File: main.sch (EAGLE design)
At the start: 108 parts, among them IC1 LD1117S50TR, IC2 LD398533RM, IC3 CP2102, IC4 PM8834-SO08N, IC5 PM8834-SO08N, J1 RJ11, Q10 IRF3205SPBF, Q11 IRF3205SPBF, Q12 IRF3205SPBF, Q13 IRF3205SPBF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

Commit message: All routed
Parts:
- removed JP3, JP4: (no value), adafruit:PINHD-1X3
- removed Q4, Q5: BSS138, SparkFun:MOSFET-NCHANNELSMD
- removed R17, R18, R19, R20: 10K, resistor:R-EU_R0805
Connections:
- removed net HV: JP2.1, JP3.1, JP4.1, R16.1, R18.1, R20.1
- removed net HV3: JP3.2, Q4.D, R18.2
- removed net HV4: JP4.2, Q5.D, R20.2
- removed net LV2: Q4.S, R17.2
- removed net LV3: Q5.S, R19.2
- net +3V3: no longer Q4.G, Q5.G, R17.1, R19.1
- net +5V: now also JP2.1, R16.1
- net GND: no longer JP3.3, JP4.3
- net LV0: now also U1.IO15
- net LV1: now also U1.IO16

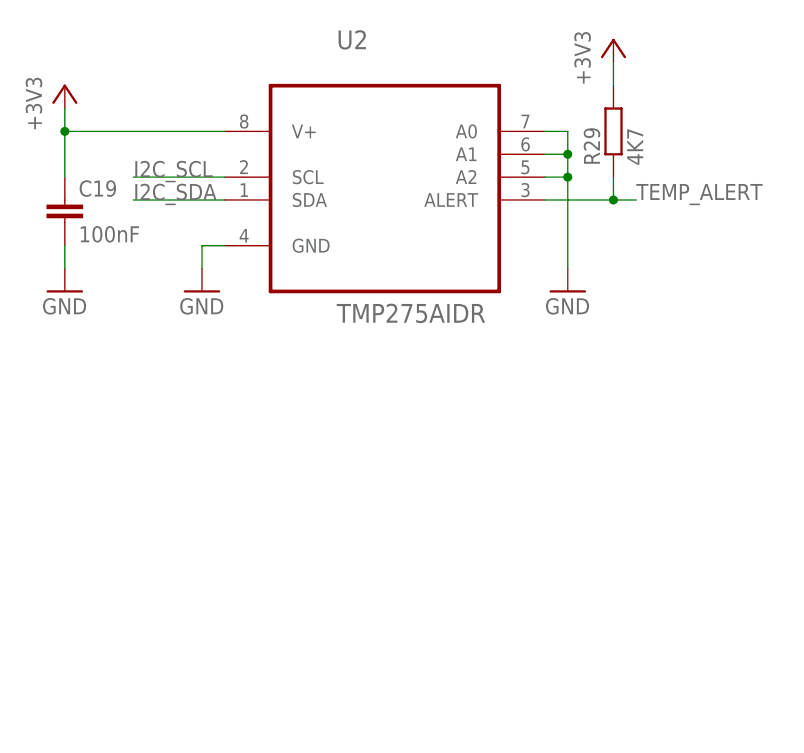
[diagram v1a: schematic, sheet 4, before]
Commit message: Added light sensor
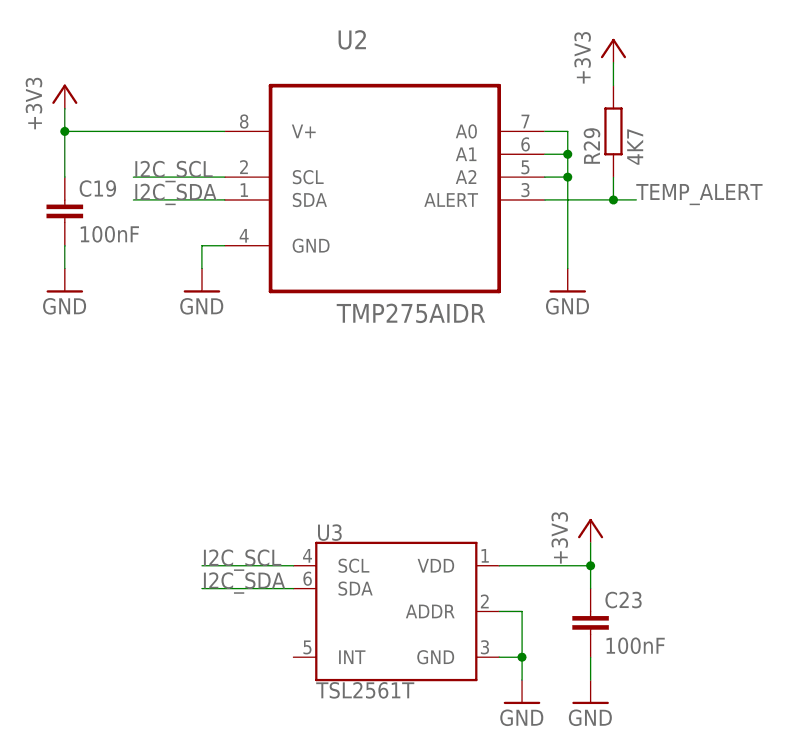
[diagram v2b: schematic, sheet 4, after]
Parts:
- added C23: 100nF, resistor:C-EUC0805
- added U3: TSL2561T, SparkFun-Sensors:TSL2561T
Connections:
- net +3V3: now also C23.1, U3.VDD
- net GND: now also C23.2, U3.ADDR, U3.GND
- net I2C_SCL: now also U3.SCL
- net I2C_SDA: now also U3.SDA
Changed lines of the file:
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@@
 <part name="P+9" library="supply1" library_urn="urn:adsk.eagle:library:371" deviceset="+5V" device=""/>
 <part name="P+5" library="supply1" library_urn="urn:adsk.eagle:library:371" deviceset="+5V" device=""/>
+<part name="U3" library="SparkFun-Sensors" library_urn="urn:adsk.eagle:library:534" deviceset="TSL2561" device="T" package3d_urn="urn:adsk.eagle:package:39968/1"/>
+<part name="GND32" library="supply1" deviceset="GND" device=""/>
+<part name="+3V1" library="supply1" deviceset="+3V3" device=""/>
+<part name="C23" library="resistor" deviceset="C-EU" device="C0805" value="100nF"/>
+<part name="GND33" library="supply1" deviceset="GND" device=""/>
 </parts>
 <sheets>
@@
 <attribute name="VALUE" x="76.2" y="60.96" size="1.778" layer="96" rot="R90"/>
 </instance>
+<instance part="U3" gate="G$1" x="53.34" y="2.54" smashed="yes">
+<attribute name="NAME" x="45.72" y="10.414" size="1.778" layer="95" font="vector"/>
+<attribute name="VALUE" x="45.72" y="-5.334" size="1.778" layer="96" font="vector" align="top-left"/>
+</instance>
+<instance part="GND32" gate="1" x="68.58" y="-7.62" smashed="yes">
+<attribute name="VALUE" x="66.04" y="-10.16" size="1.778" layer="96"/>
+</instance>
+<instance part="+3V1" gate="G$1" x="76.2" y="12.7" smashed="yes">
+<attribute name="VALUE" x="73.66" y="7.62" size="1.778" layer="96" rot="R90"/>
+</instance>
+<instance part="C23" gate="G$1" x="76.2" y="2.54" smashed="yes">
+<attribute name="NAME" x="77.724" y="2.921" size="1.778" layer="95"/>
+<attribute name="VALUE" x="77.724" y="-2.159" size="1.778" layer="96"/>
+</instance>
+<instance part="GND33" gate="1" x="76.2" y="-7.62" smashed="yes">
+<attribute name="VALUE" x="73.66" y="-10.16" size="1.778" layer="96"/>
+</instance>
 </instances>
 <busses>
@@
 <pinref part="GND44" gate="1" pin="GND"/>
 </segment>
+<segment>
+<pinref part="U3" gate="G$1" pin="ADDR"/>
+<wire x1="66.04" y1="2.54" x2="68.58" y2="2.54" width="0.1524" layer="91"/>
+<wire x1="68.58" y1="2.54" x2="68.58" y2="-2.54" width="0.1524" layer="91"/>
+<pinref part="U3" gate="G$1" pin="GND"/>
+<wire x1="68.58" y1="-2.54" x2="68.58" y2="-5.08" width="0.1524" layer="91"/>
+<wire x1="66.04" y1="-2.54" x2="68.58" y2="-2.54" width="0.1524" layer="91"/>
+<junction x="68.58" y="-2.54"/>
+<pinref part="GND32" gate="1" pin="GND"/>
+</segment>
+<segment>
+<pinref part="GND33" gate="1" pin="GND"/>
+<pinref part="C23" gate="G$1" pin="2"/>
+<wire x1="76.2" y1="-2.54" x2="76.2" y2="-5.08" width="0.1524" layer="91"/>
+</segment>
 </net>
 <net name="+3V3" class="0">
@@
 <pinref part="+3V320" gate="G$1" pin="+3V3"/>
 </segment>
+<segment>
+<pinref part="U3" gate="G$1" pin="VDD"/>
+<wire x1="66.04" y1="7.62" x2="76.2" y2="7.62" width="0.1524" layer="91"/>
+<wire x1="76.2" y1="7.62" x2="76.2" y2="10.16" width="0.1524" layer="91"/>
+<pinref part="+3V1" gate="G$1" pin="+3V3"/>
+<pinref part="C23" gate="G$1" pin="1"/>
+<wire x1="76.2" y1="5.08" x2="76.2" y2="7.62" width="0.1524" layer="91"/>
+<junction x="76.2" y="7.62"/>
+</segment>
 </net>
 <net name="I2C_SDA" class="0">
@@
 <label x="25.4" y="48.26" size="1.778" layer="95"/>
 </segment>
+<segment>
+<wire x1="33.02" y1="5.08" x2="43.18" y2="5.08" width="0.1524" layer="91"/>
+<pinref part="U3" gate="G$1" pin="SDA"/>
+<label x="33.02" y="5.08" size="1.778" layer="95"/>
+</segment>
 </net>
 <net name="I2C_SCL" class="0">
@@
 <label x="25.4" y="50.8" size="1.778" layer="95"/>
 </segment>
-</net>
+<segment>
+<wire x1="43.18" y1="7.62" x2="33.02" y2="7.62" width="0.1524" layer="91"/>
+<pinref part="U3" gate="G$1" pin="SCL"/>
+<label x="33.02" y="7.62" size="1.778" layer="95"/>
+</segment>
+</net>

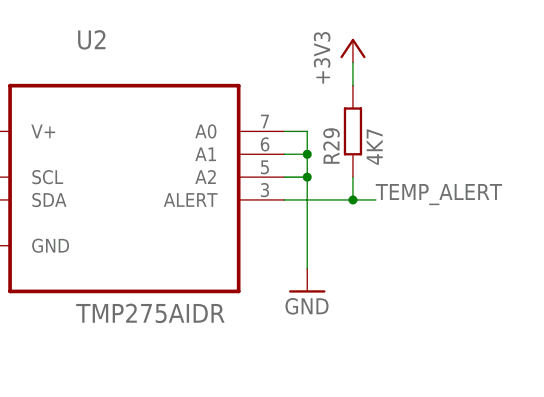
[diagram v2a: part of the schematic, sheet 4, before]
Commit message: Removed temp alert signal
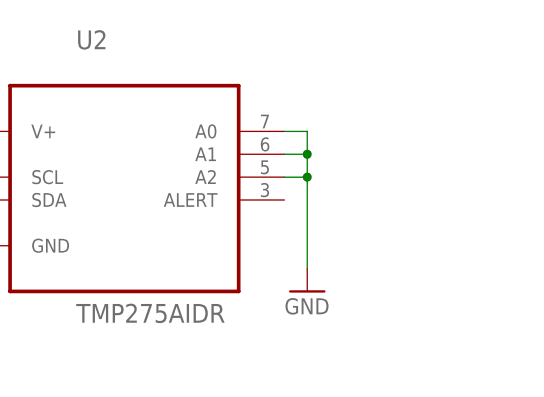
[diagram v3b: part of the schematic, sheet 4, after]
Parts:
- removed R29: 4K7, resistor:R-EU_R0805
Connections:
- removed net TEMP_ALERT: R29.1, U1.IO21, U2.ALERT
- net +3V3: no longer R29.2
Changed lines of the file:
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@@
 <part name="+3V39" library="supply1" library_urn="urn:adsk.eagle:library:371" deviceset="+3V3" device=""/>
 <part name="+3V310" library="supply1" library_urn="urn:adsk.eagle:library:371" deviceset="+3V3" device=""/>
-<part name="R29" library="resistor" library_urn="urn:adsk.eagle:library:348" deviceset="R-EU_" device="R0805" package3d_urn="urn:adsk.eagle:package:23553/2" value="4K7"/>
-<part name="+3V320" library="supply1" deviceset="+3V3" device=""/>
 <part name="GND25" library="supply1" library_urn="urn:adsk.eagle:library:371" deviceset="GND" device=""/>
 <part name="GND26" library="supply1" library_urn="urn:adsk.eagle:library:371" deviceset="GND" device=""/>
@@
 </segment>
 </net>
-<net name="TEMP_ALERT" class="0">
-<segment>
-<pinref part="U1" gate="G$1" pin="IO21"/>
-<wire x1="149.86" y1="73.66" x2="157.48" y2="73.66" width="0.1524" layer="91"/>
-<label x="154.94" y="73.66" size="1.778" layer="95"/>
-</segment>
-</net>
 <net name="INP2" class="0">
 <segment>
@@
 <instance part="GND44" gate="1" x="73.66" y="38.1" smashed="yes">
 <attribute name="VALUE" x="71.12" y="35.56" size="1.778" layer="96"/>
-</instance>
-<instance part="R29" gate="G$1" x="78.74" y="55.88" smashed="yes" rot="R90">
-<attribute name="NAME" x="77.2414" y="52.07" size="1.778" layer="95" rot="R90"/>
-<attribute name="VALUE" x="82.042" y="52.07" size="1.778" layer="96" rot="R90"/>
-</instance>
-<instance part="+3V320" gate="G$1" x="78.74" y="66.04" smashed="yes">
-<attribute name="VALUE" x="76.2" y="60.96" size="1.778" layer="96" rot="R90"/>
 </instance>
 <instance part="U3" gate="G$1" x="53.34" y="2.54" smashed="yes">
@@
 </segment>
 <segment>
-<pinref part="R29" gate="G$1" pin="2"/>
-<wire x1="78.74" y1="60.96" x2="78.74" y2="63.5" width="0.1524" layer="91"/>
-<pinref part="+3V320" gate="G$1" pin="+3V3"/>
-</segment>
-<segment>
 <pinref part="U3" gate="G$1" pin="VDD"/>
 <wire x1="66.04" y1="7.62" x2="76.2" y2="7.62" width="0.1524" layer="91"/>
@@
 </segment>
 </net>
-<net name="TEMP_ALERT" class="0">
-<segment>
-<pinref part="U2" gate="A" pin="ALERT"/>
-<wire x1="71.12" y1="48.26" x2="78.74" y2="48.26" width="0.1524" layer="91"/>
-<label x="81.28" y="48.26" size="1.778" layer="95"/>
-<pinref part="R29" gate="G$1" pin="1"/>
-<wire x1="78.74" y1="48.26" x2="81.28" y2="48.26" width="0.1524" layer="91"/>
-<wire x1="78.74" y1="48.26" x2="78.74" y2="50.8" width="0.1524" layer="91"/>
-<junction x="78.74" y="48.26"/>
-</segment>
-</net>

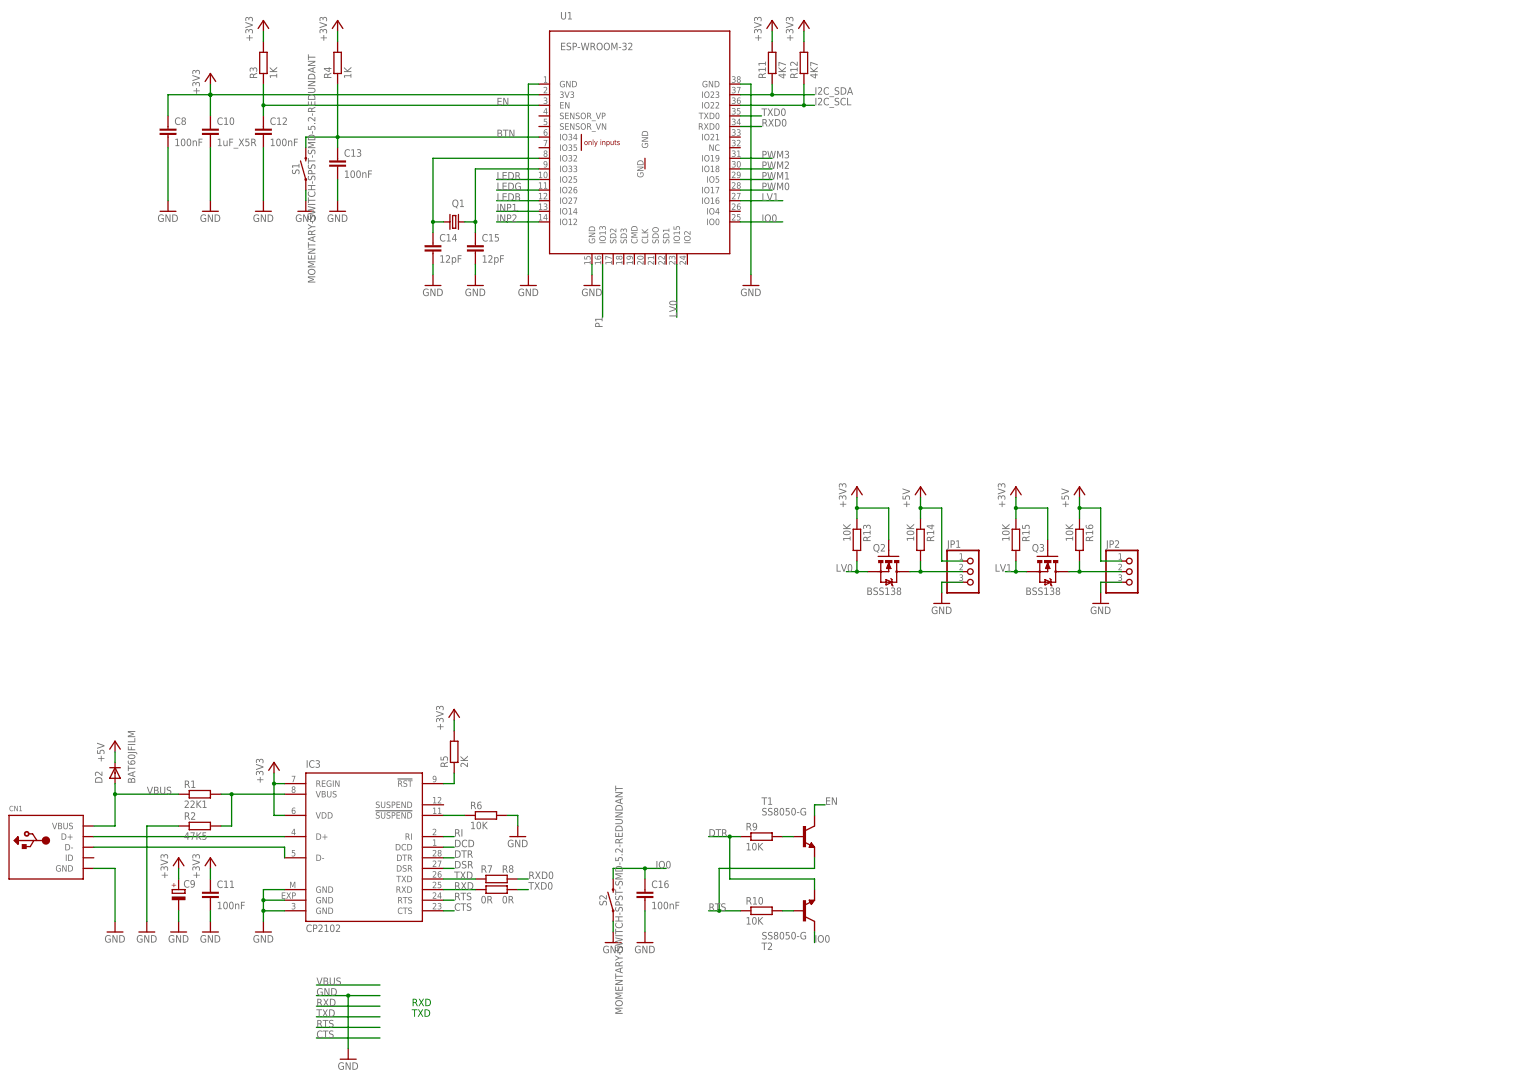
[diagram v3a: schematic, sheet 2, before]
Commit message: Replaced usb chip by connector
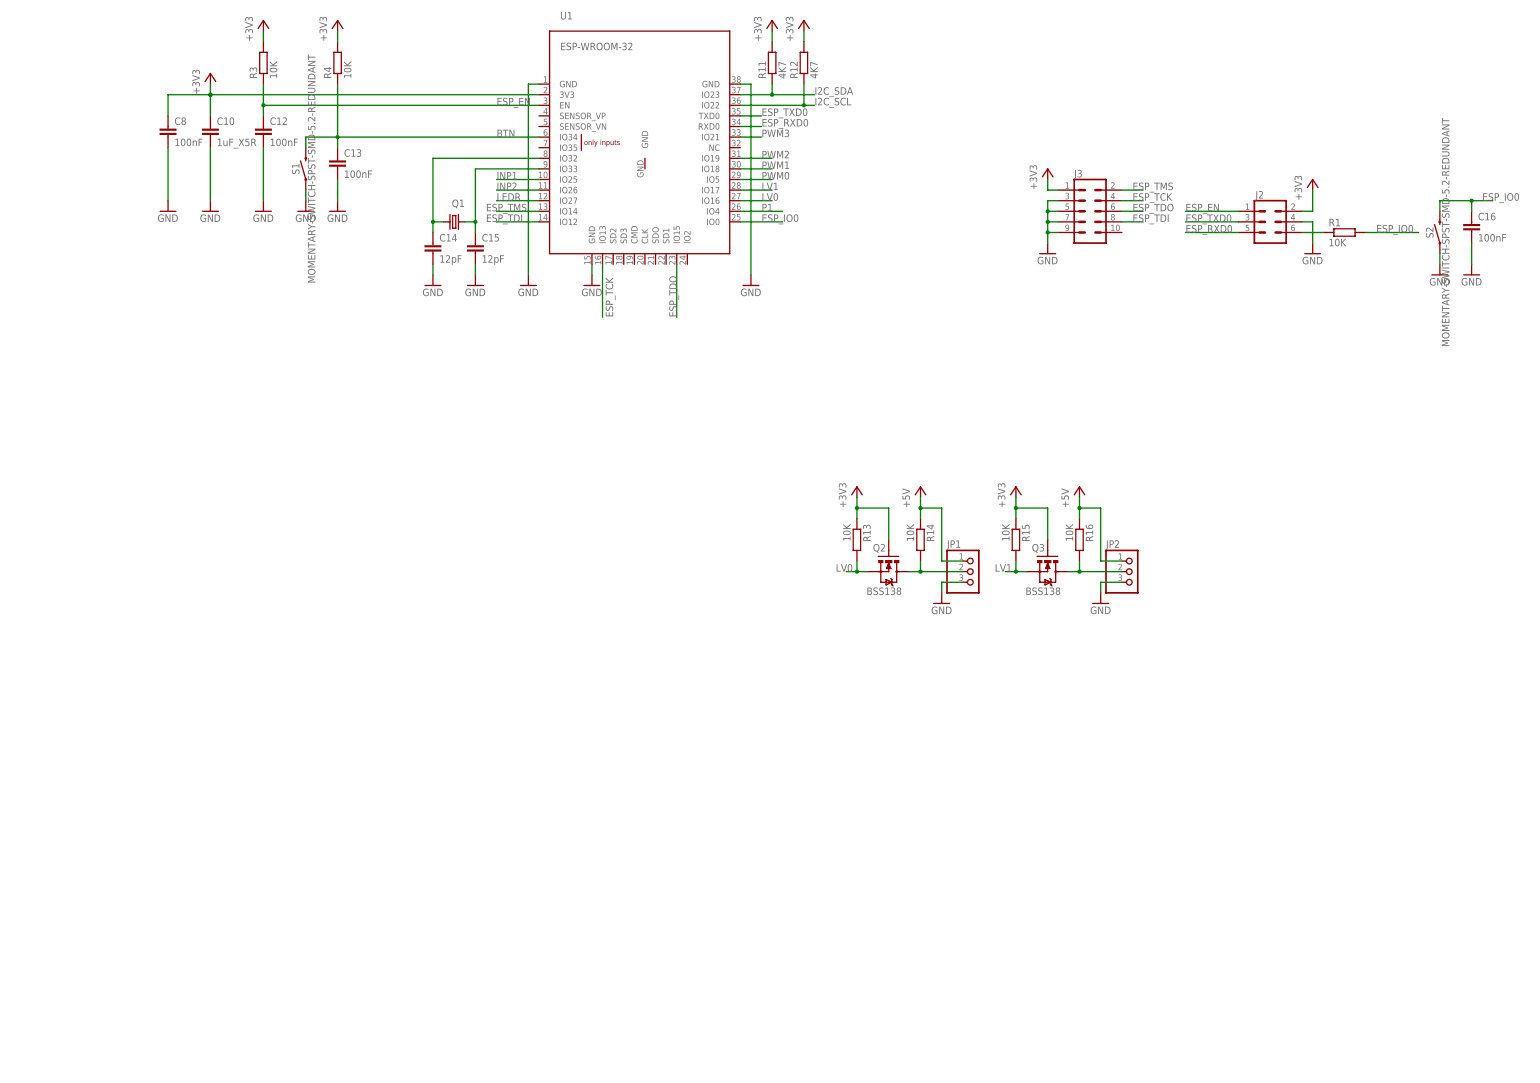
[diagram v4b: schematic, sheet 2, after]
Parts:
- removed C11: 100nF, resistor:C-EUC0805
- removed C9: (no value), resistor:CPOL-EUSMCA
- removed CN1: (no value), adafruit:USBMINIB
- removed D2: BAT60JFILM, diode:DIODE-SOD323-W
- removed IC3: CP2102, silabs:CP2102
- removed Q7, Q8: BSS138, SparkFun:MOSFET-NCHANNELSMD
- removed R10, R31, R32, R6, R9: 10K, resistor:R-EU_R0805
- removed R2: 47K5, resistor:R-EU_R0805
- removed R5: 2K, resistor:R-EU_R0805
- removed R7, R8: 0R, resistor:R-EU_R0805
- removed T1, T2: SS8050-G, transistor:BCF29-NPN-SOT23-BEC
- added J2: (no value), SparkFun-Connectors:CONN_03X2SHROUD
- added J3: (no value), SparkFun-Connectors:CONN_05X2SHD
- LED1: value RGBLED5050 -> RED; device adafruit:RGBLED5050 -> led:LEDCHIPLED_0805
- R1: value 22K1 -> 10K
- R3, R4: value 1K -> 10K
- R30: value 10K -> 1K
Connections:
- removed net CTS: IC3.CTS
- removed net DCD: IC3.DCD
- removed net DSR: IC3.DSR
- removed net DTR: IC3.DTR, R9.1, T2.E
- removed net EN: C12.1, R3.1, T1.C, U1.EN
- removed net IO0: C16.1, S2.2, T2.C, U1.IO0
- removed net LEDB: Q8.G, U1.IO27
- removed net LEDG: Q7.G, U1.IO26
- removed net N$11: LED1.RED_C, R31.1
- removed net N$19: IC3.!SUSPEND, R6.1
- removed net N$21: IC3.!RST, R5.1
- removed net N$24: IC3.VBUS, R1.2, R2.2
- removed net N$25: CN1.D-, IC3.D-
- removed net N$29: LED1.BLUE_C, R32.1
- removed net N$31: Q7.D, R31.2
- removed net N$32: Q8.D, R32.2
- removed net N$42: R9.2, T1.B
- removed net N$43: R10.2, T2.B
- removed net N$6: CN1.D+, IC3.D+
- removed net RI: IC3.RI
- removed net RTS: IC3.RTS, R10.1, T1.E
- removed net RXD: IC3.RXD, R8.1
- removed net RXD0: R7.2, U1.RXD0
- removed net TXD: IC3.TXD, R7.1
- removed net TXD0: R8.2, U1.TXD0
- removed net VBUS: CN1.VBUS, D2.A, R1.1
- new net ESP_EN: C12.1, J2.1, R3.1, U1.EN
- new net ESP_IO0: C16.1, R1.2, S2.2, U1.IO0
- new net ESP_RXD0: J2.5, U1.RXD0
- new net ESP_TCK: J3.4, U1.IO13
- new net ESP_TDI: J3.8, U1.IO12
- new net ESP_TDO: J3.6, U1.IO15
- new net ESP_TMS: J3.2, U1.IO14
- new net ESP_TXD0: J2.3, U1.TXD0
- new net N$4: J2.6, R1.1
- net +3V3: now also J2.2, J3.1, LED1.A; no longer C11.1, C9.+, IC3.REGIN, IC3.VDD, LED1.BLUE_A, LED1.GREEN_A, LED1.RED_A, R5.2
- net +5V: no longer D2.C
- net GND: now also J2.4, J3.3, J3.5, J3.7, J3.9; no longer C11.2, C9.-, CN1.GND, IC3.GND, IC3.GND@EXP, IC3.GND@M, Q7.S, Q8.S, R2.1, R6.2
- net INP1: now also U1.IO25; no longer U1.IO14
- net INP2: now also U1.IO26; no longer U1.IO12
- net LEDR: now also U1.IO27; no longer U1.IO25
- net LV0: now also U1.IO16; no longer U1.IO15
- net LV1: now also U1.IO17; no longer U1.IO16
- net N$5: now also LED1.C; no longer LED1.GREEN_C
- net P1: now also U1.IO4; no longer U1.IO13
- net PWM0: now also U1.IO5; no longer U1.IO17
- net PWM1: now also U1.IO18; no longer U1.IO5
- net PWM2: now also U1.IO19; no longer U1.IO18
- net PWM3: now also U1.IO21; no longer U1.IO19
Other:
- note removed: "RXD"
- note removed: "TXD"
- moved on the sheet: C16, R1, S2
